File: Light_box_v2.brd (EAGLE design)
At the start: 101.8 x 82.3 mm, 35 parts, among them IC1 ATMEGA328-PU, U1 OPA1671IDBVR

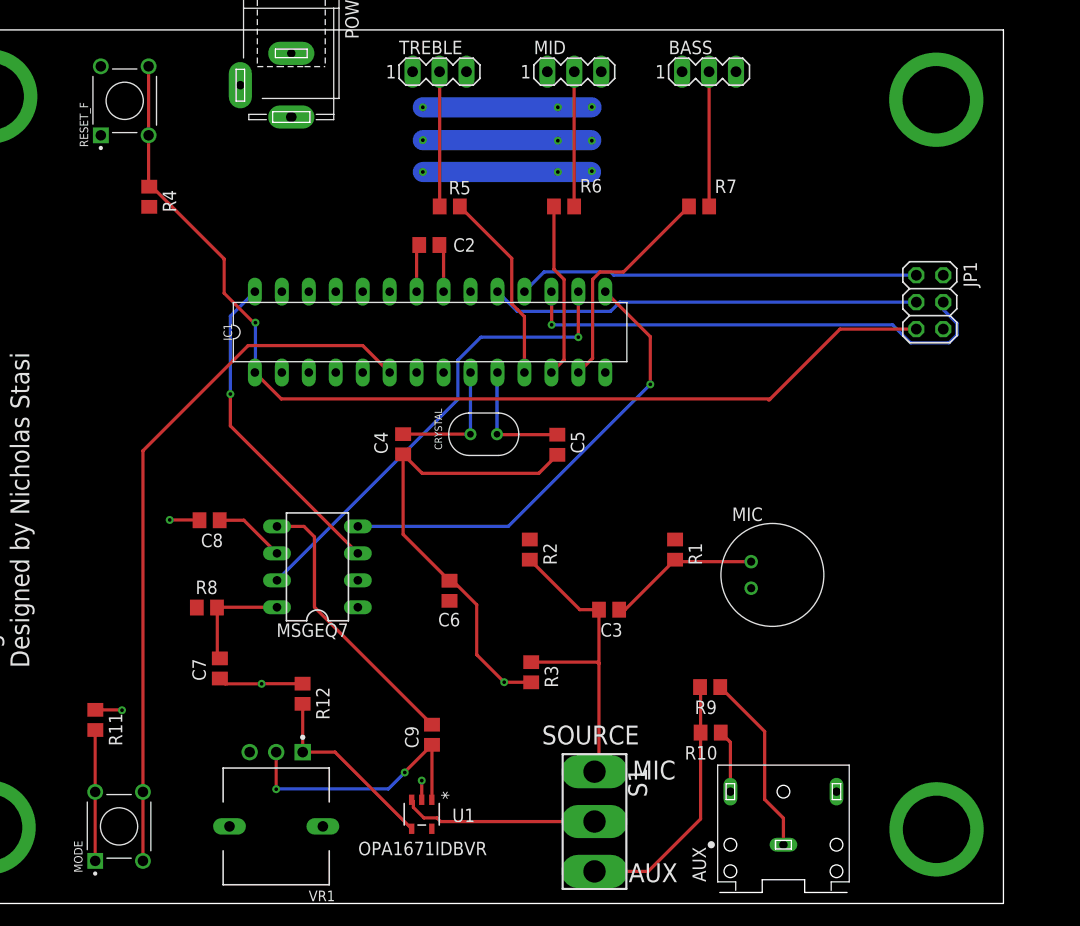
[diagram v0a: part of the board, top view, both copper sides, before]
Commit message: Adding some datasheets. Corrected error in mode button and added values to components
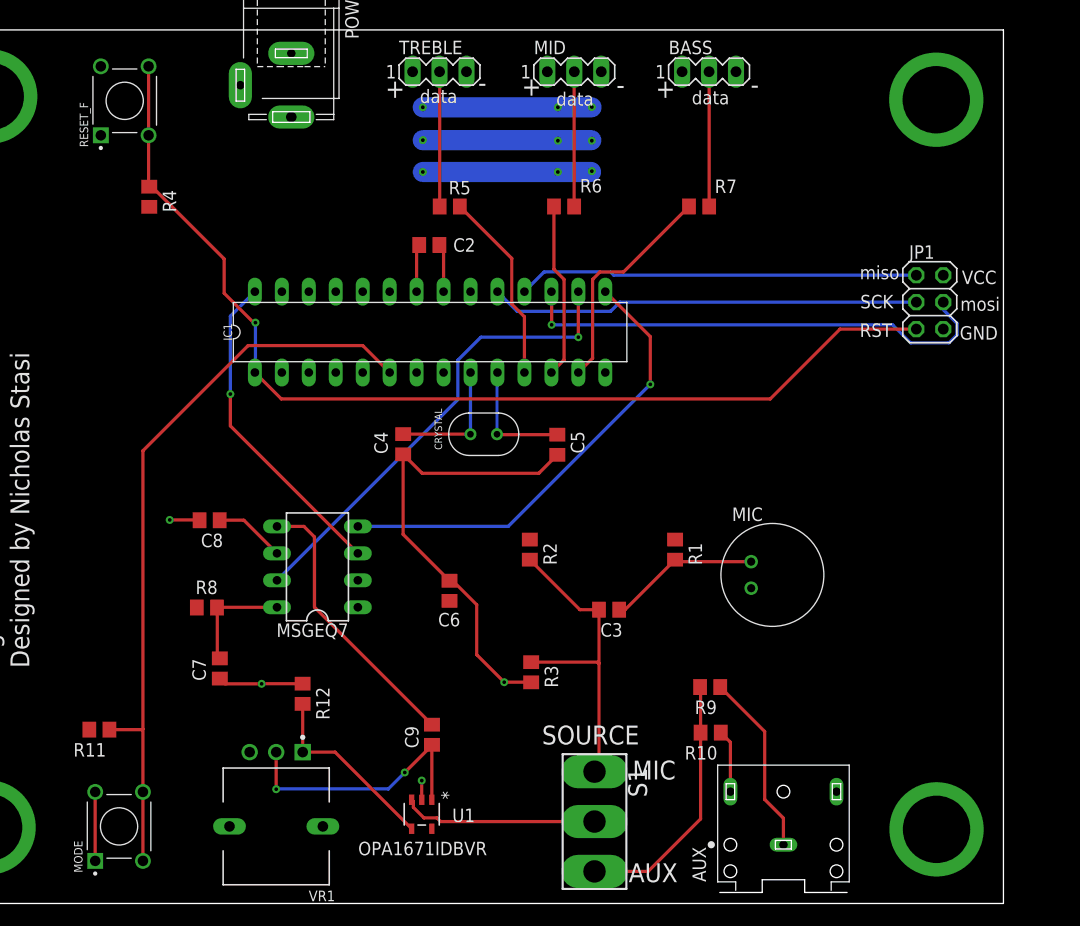
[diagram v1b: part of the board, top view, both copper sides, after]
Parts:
- C2, C6, C8: value (none) -> 0.1uF
- C3: value (none) -> 1uF
- C4, C5: value (none) -> 22pF
- C7: value (none) -> 33pF
- C9: value (none) -> 10uF
- R1: value (none) -> 2.2k
- R10, R9: value (none) -> 22k
- R11, R2, R3, R4: value (none) -> 10k
- R12: value (none) -> 500
- R5, R6, R7: value (none) -> 220
- R8: value (none) -> 200k
- moved R11 0.99 mm to (22.7, 26.5), turned to 180 degrees
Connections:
- removed net N$17: MODE.1, MODE.2, R11.2
- net GND: now also MODE.1, MODE.2; no longer R11.1
- net N$22: now also R11.1
- net VCC: now also R11.2
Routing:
- net N$17: track 12.4 -> 0.00 mm
- net GND: track 63.8 -> 67.8 mm, vias 5 -> 4
- net N$22: track 67.1 -> 70.2 mm
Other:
- board text added: "+"
- board text added: "-"
- board text added: "GND"
- board text added: "RST"
- board text added: "SCK"
- board text added: "VCC"
- board text added: "data"
- board text added: "miso"
- board text added: "mosi"
